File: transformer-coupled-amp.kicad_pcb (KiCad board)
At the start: 2 copper layers, 49 parts, among them J1 DIN-3, Q1 МП41А, Q2 МП41А, Q3 МП25Б, Q4 МП25Б, Q5 МП37А, Q6 МП40A, Q7 МП37А, Q8 П213Б, Q9 П213Б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

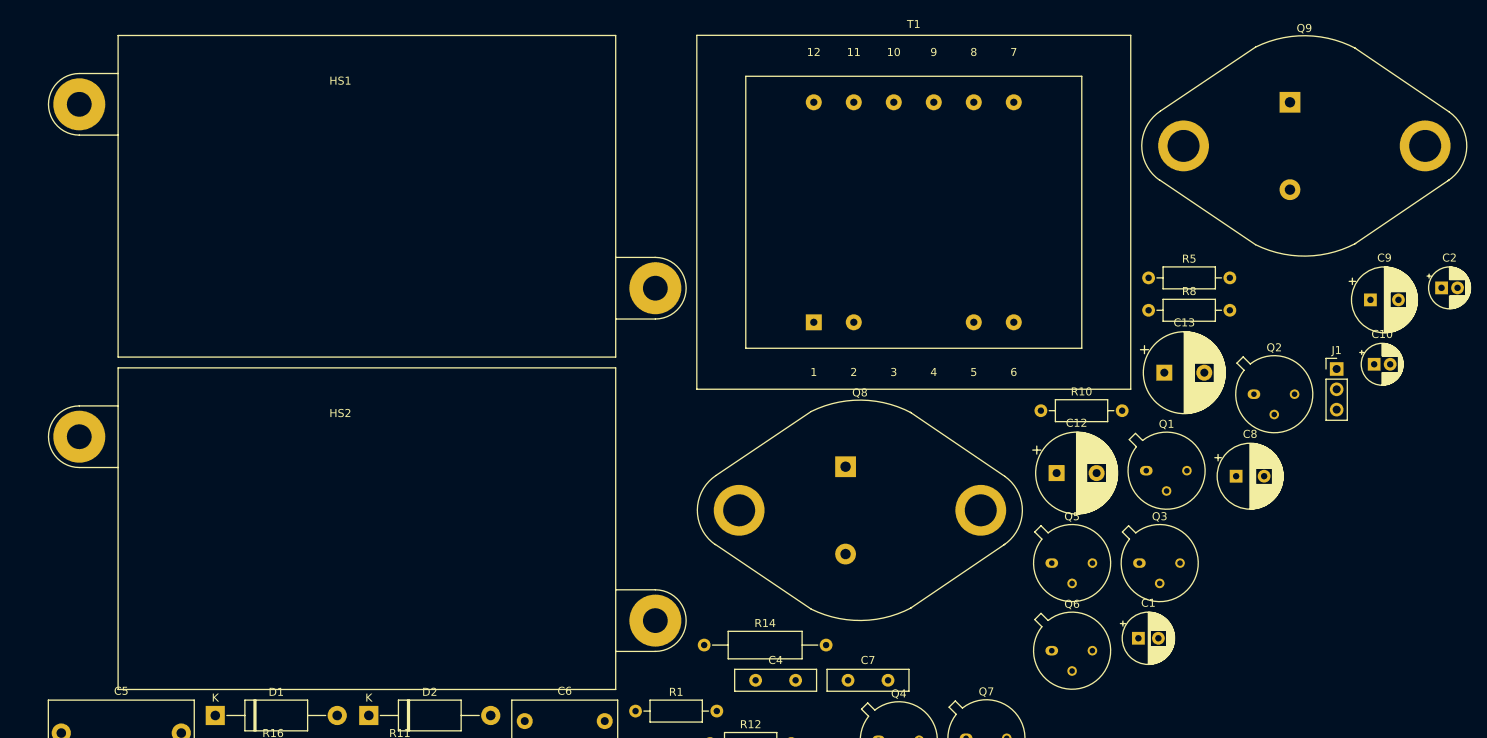
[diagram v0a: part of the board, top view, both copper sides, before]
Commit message: Add transformer footrpint
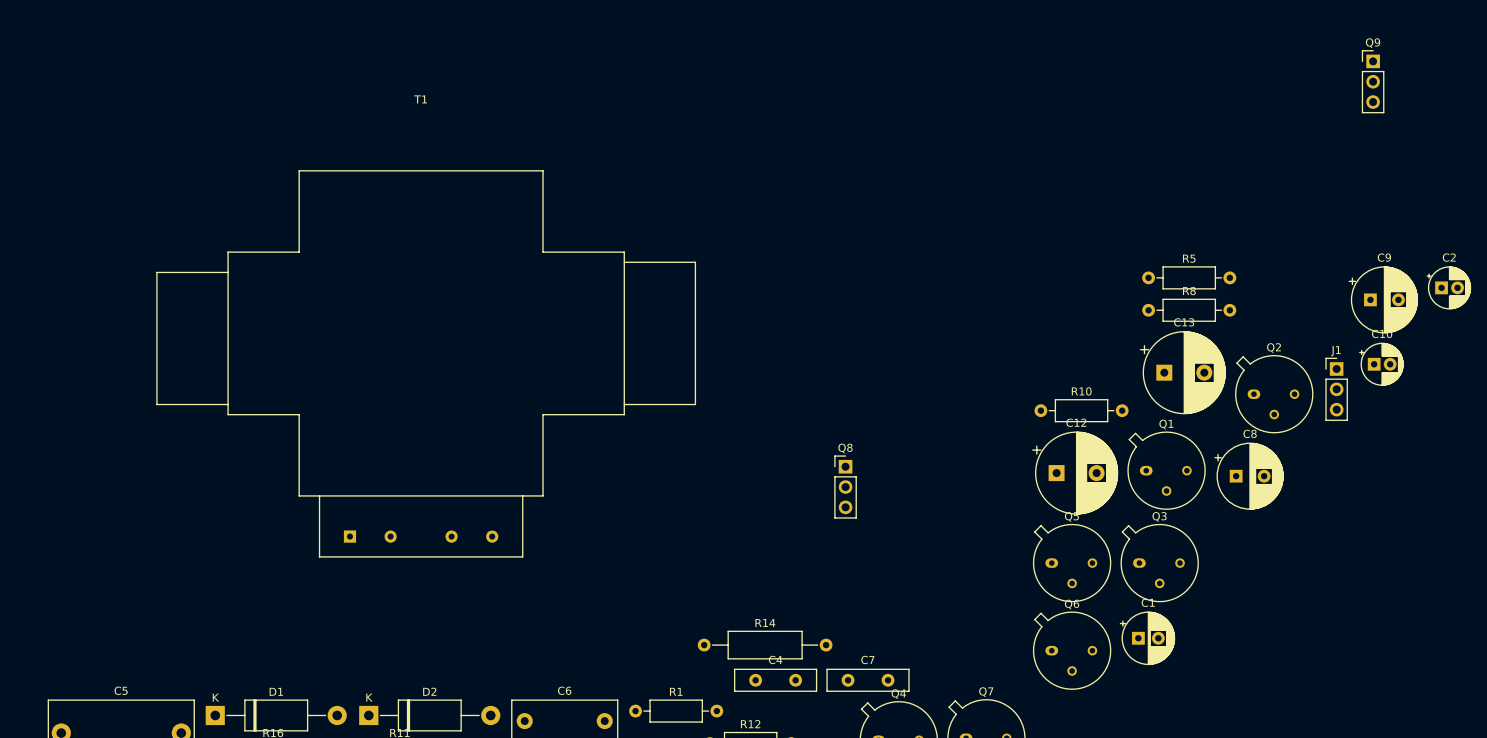
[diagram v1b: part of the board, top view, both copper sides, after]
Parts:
- removed HS1, HS2: Heatsink, Heatsink:Heatsink_62x40mm_2xFixation3mm
- Q8, Q9: footprint Package_TO_SOT_THT:TO-3 -> Connector_PinHeader_2.54mm:PinHeader_1x03_P2.54mm_Vertical
- T1: footprint Transformer_THT:Transformer_Breve_TEZ-44x52 -> footprints:Transformer_44x40
- moved T1 49.1 mm to (111.0, 80.0)
- moved Q9 11.6 mm to (230.0, 46.0)

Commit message: Finish toneblock placement
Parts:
- moved T1 271.3 mm to (382.3, 80.0), turned to 90 degrees
- moved J1 206.2 mm to (21.6, 115.6)
- moved C2 200.2 mm to (45.7, 128.3), turned to 90 degrees
- moved Q1 145.9 mm to (59.7, 130.8), turned to 90 degrees
- moved Q5 144.6 mm to (328.3, 66.8)
- moved Q6 144.6 mm to (328.3, 77.8)
- moved C11 144.6 mm to (304.3, 97.8)
- moved C13 144.6 mm to (342.3, 43.0)
- moved C8 144.6 mm to (351.3, 55.9)
- moved D1 144.6 mm to (223.7, 85.8)
- moved D2 144.6 mm to (242.9, 85.8)
- moved LS1 144.6 mm to (299.6, 96.9)
- moved Q3 144.6 mm to (339.2, 66.8)
- moved Q4 144.6 mm to (306.6, 89.0)
- moved Q8 144.6 mm to (302.5, 54.8)
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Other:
- net class Power added: clearance 0.3, trace_width 1, via_dia 0.8, via_drill 0.4

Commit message: Route preamp
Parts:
- moved R5 318.4 mm to (30.5, 104.1)
- moved C1 292.2 mm to (48.3, 104.1), turned to 180 degrees
- moved C9 257.5 mm to (129.5, 130.8), turned to 90 degrees
- moved Q3 252.5 mm to (94.0, 127.0), turned to 270 degrees
- moved R10 244.6 mm to (88.9, 104.1)
- moved C8 230.3 mm to (129.5, 118.1), turned to 90 degrees
- moved Q5 222.5 mm to (115.6, 132.1), turned to 90 degrees
- moved Q4 195.8 mm to (113.0, 118.1)
- moved R12 189.5 mm to (102.9, 139.7), turned to 180 degrees
- moved T1 166.3 mm to (226.1, 137.2)
- moved R11 161.7 mm to (87.6, 139.7), turned to 180 degrees
- moved D1 123.5 mm to (104.1, 116.8), turned to 270 degrees
- moved Q2 16.5 mm to (94.0, 115.6), turned to 270 degrees
- moved R3 12.7 mm to (43.2, 110.5)
- moved J1 8.98 mm to (22.9, 124.5), turned to 180 degrees
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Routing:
- net -24V: track 0.00 -> 163.7 mm
- net Net-(C5-Pad2): track 0.00 -> 34.7 mm
- net Net-(C4-Pad1): track 0.00 -> 31.8 mm
- net Net-(D1-Pad1): track 0.00 -> 31.8 mm
- net GND: track 0.00 -> 31.8 mm
- net Net-(C6-Pad1): track 0.00 -> 29.5 mm
- net Net-(C3-Pad2): track 0.00 -> 27.5 mm
- net Net-(Q2-Pad3): track 0.00 -> 25.0 mm
- net Net-(Q2-Pad2): track 0.00 -> 23.2 mm
- net Net-(C2-Pad2): track 0.00 -> 20.7 mm
- net Net-(D1-Pad2): track 0.00 -> 19.6 mm
- net Net-(C1-Pad2): track 0.00 -> 18.9 mm
- net Net-(C3-Pad1): track 0.00 -> 18.6 mm
- net Net-(J1-Pad3): track 0.00 -> 14.3 mm
- net Net-(Q4-Pad2): track 0.00 -> 14.3 mm
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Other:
- net class Default: clearance 0.2 -> 0.3; trace_width 0.25 -> 0.35
- rule trace_clearance: 0.2 -> 0.3

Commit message: Finish pcb routing
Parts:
- moved Q9 295.3 mm to (86.4, 91.4), turned to 180 degrees
- moved C13 268.2 mm to (77.5, 85.1), turned to 180 degrees
- moved C12 260.8 mm to (72.4, 102.9)
- moved C10 232.7 mm to (139.7, 83.8), turned to 180 degrees
- moved LS1 223.4 mm to (76.2, 94.0), turned to 270 degrees
- moved Q8 221.4 mm to (86.4, 102.9), turned to 180 degrees
- moved Q7 215.2 mm to (102.9, 102.9), turned to 180 degrees
- moved Q6 205.2 mm to (124.5, 101.6), turned to 180 degrees
- moved C11 166.0 mm to (139.7, 76.2), turned to 180 degrees
- moved R14 155.5 mm to (129.5, 85.1), turned to 180 degrees
- moved D2 128.7 mm to (114.3, 91.4)
- moved R13 127.2 mm to (114.3, 80.0)
- moved R16 115.4 mm to (108.0, 86.4), turned to 180 degrees
- moved R17 111.1 mm to (92.7, 92.7)
- moved T1 95.8 mm to (175.3, 55.9), turned to 270 degrees
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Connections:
- C1 pad 1: GND -> GND1
- C13 pad 1: GND -> GND2
- C7 pad 2: GND -> GND1
- C9 pad 1: GND -> GND1
- J1 pad 2: GND -> GND1
- Q5 pad 3: GND -> GND1
- Q9 pad 2: GND -> GND2
- R11 pad 2: GND -> GND1
- R12 pad 2: GND -> GND1
- R15 pad 2: GND -> GND2
- R17 pad 2: GND -> GND2
- R4 pad 2: GND -> GND1
- R7 pad 2: GND -> GND1
- RV1 pad 3: GND -> GND1
- T1 pad 3: GND -> GND2
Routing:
- net GND1: track 0.00 -> 94.5 mm
- net -24V: track 163.7 -> 258.0 mm
- net GND2: track 0.00 -> 92.5 mm
- net Net-(Q6-Pad2): track 0.00 -> 70.6 mm
- net Net-(LS1-Pad1): track 0.00 -> 68.9 mm
- net Net-(C11-Pad2): track 0.00 -> 60.8 mm
- net Net-(Q4-Pad2): track 14.3 -> 66.8 mm
- net Net-(C10-Pad2): track 0.00 -> 49.3 mm
- net GND: track 31.8 -> 0.00 mm
- net Net-(C10-Pad1): track 0.00 -> 24.7 mm
- net Net-(Q7-Pad3): track 0.00 -> 19.1 mm
- net Net-(C12-Pad1): track 0.00 -> 18.8 mm
- net Net-(D1-Pad2): track 19.6 -> 34.7 mm
- net Net-(C5-Pad2): track 34.7 -> 49.6 mm
- net Net-(C8-Pad1): track 9.20 -> 23.2 mm
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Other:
- board outline added: 188 x 96.5 mm
- net class Power: trace_width 1 -> 0.8
- rule trace_min: 0.2 -> 0
